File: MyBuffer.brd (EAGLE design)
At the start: 60 x 137.5 mm, 72 parts, among them Q1 BD140, Q2 BD139, Q3 BD140, Q4 BD139, T10 BD140, T11 BD139, T12 BD140, T9 BD139

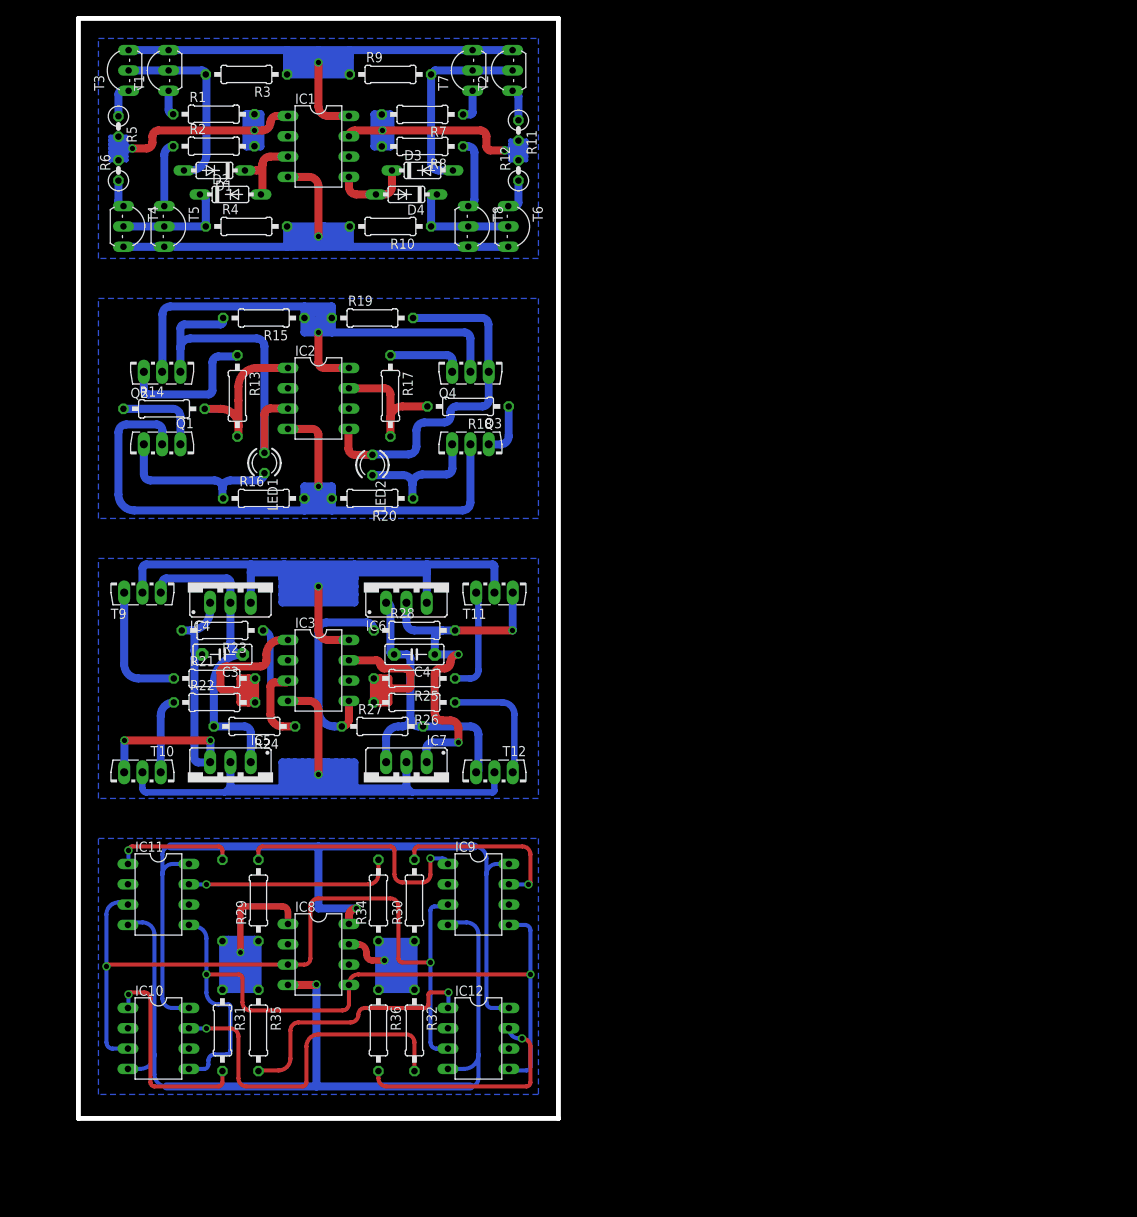
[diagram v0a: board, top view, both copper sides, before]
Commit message: add module capacitance multiplier and buffer ground
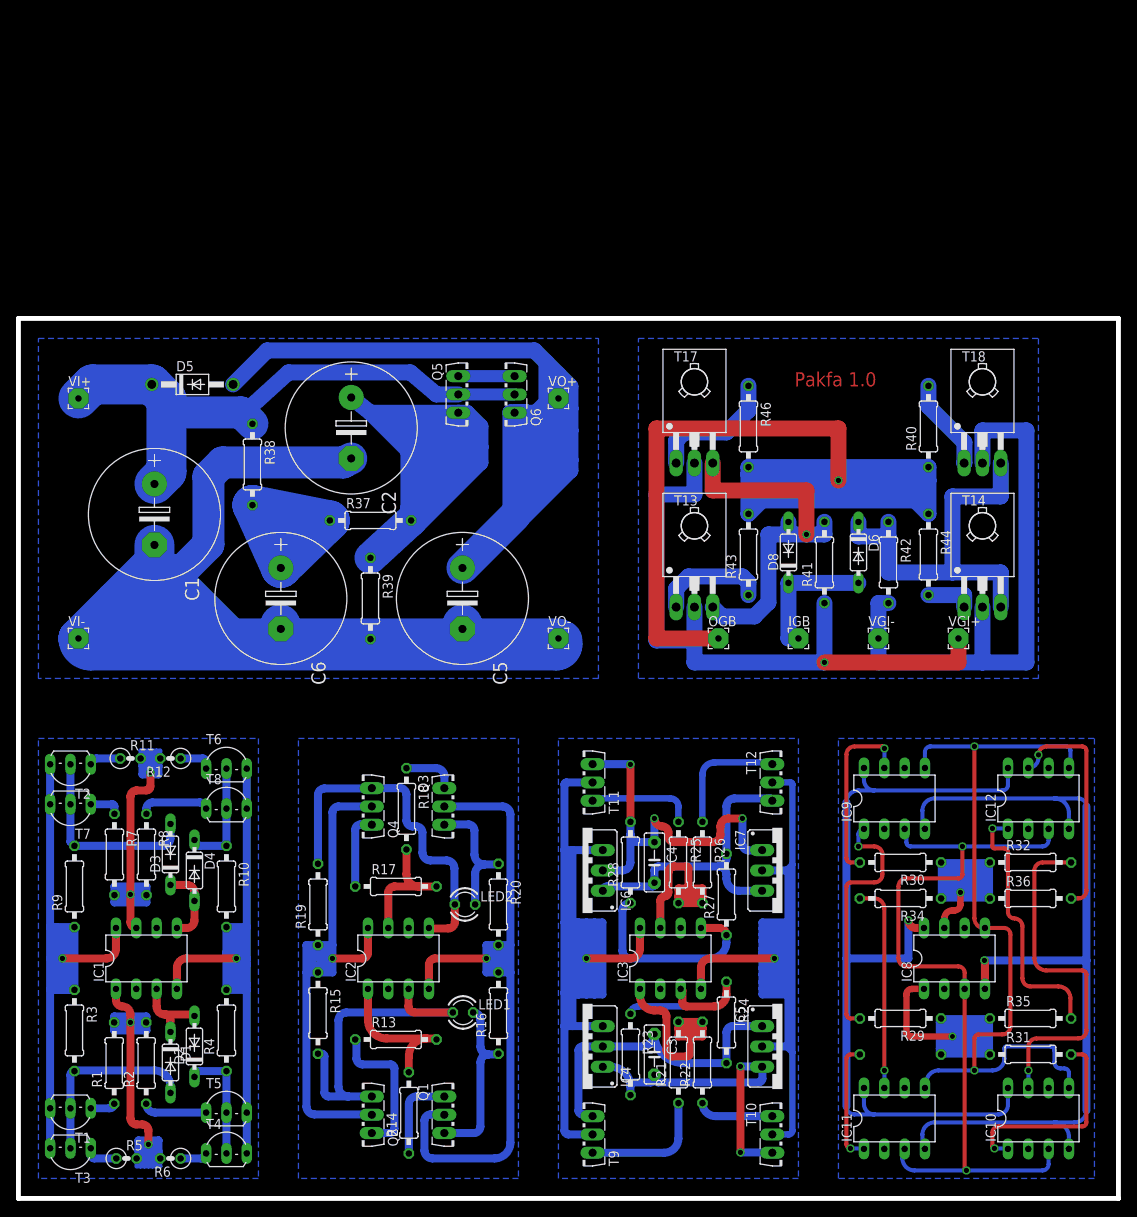
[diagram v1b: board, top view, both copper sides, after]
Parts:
- added C1: 2200uf, rcl:E7,5-16
- added C2, C5, C6: 470uf, rcl:E7,5-16
- added D5: 1N4004, diode:DO41-10
- added D6, D8: 1N4148DO35-7, diode:DO35-7
- added IGB, OGB, VGI+, VGI-, VI+, VI-, VO+, VO-: (no value), wirepad:2,54/0,8
- added Q5, Q6: BD139, transistor-power:TO126AV
- added R37, R38: 220, resistor:0207/10
- added R39: 12k, resistor:0207/10
- added R40, R43, R44, R46: 10, resistor:0207/10
- added R41, R42: 2k, resistor:0207/10
- added T13, T17: BD139, transistor-npn:TO126
- added T14, T18: BD140, transistor-pnp:TO126
- moved T3 136.1 mm to (-1.00, -5.00), turned to 180 degrees
- moved T1 131.5 mm to (-1.00, 0.00), turned to 180 degrees
- moved R5 129.0 mm to (6.00, -5.00), turned to 0 degrees
- moved R6 123.7 mm to (11.5, -5.00), turned to 180 degrees
- moved R3 121.4 mm to (-0.50, 11.0), turned to 270 degrees
- moved R1 119.3 mm to (4.47, 6.92), turned to 90 degrees
- moved T4 115.2 mm to (18.5, -3.10), turned to 0 degrees
- moved R2 114.9 mm to (8.47, 6.92), turned to 90 degrees
- moved D1 111.6 mm to (11.5, 7.00), turned to 270 degrees
- moved IC10 110.5 mm to (120.0, 0.00), turned to 0 degrees
- moved T5 109.7 mm to (18.5, 2.00), turned to 0 degrees
- moved R9 108.9 mm to (-0.50, 29.0), turned to 90 degrees
- moved D2 106.6 mm to (14.5, 9.00), turned to 90 degrees
- moved T7 105.1 mm to (-1.00, 38.0), turned to 180 degrees
- moved IC1 103.8 mm to (8.50, 20.0), turned to 0 degrees
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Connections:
- new net N$32: C2.+, Q5.B, R37.2, R39.1
- new net N$33: Q5.E, Q6.B
- new net N$35: C6.+, R37.1, R38.2
- new net N$36: C1.+, D5.C, Q5.C, Q6.C, R38.1, VI+.1
- new net N$37: C1.-, C2.-, C5.-, C6.-, R39.2, VI-.1, VO-.1
- new net N$39: C5.+, D5.A, Q6.E, VO+.1
- new net N$40: OGB.1, R40.1, R43.2, R44.1, R46.2
- new net N$42: R46.1, T17.1
- new net N$44: R40.2, T18.1
- new net N$45: D6.C, R42.1, T14.3, T18.3
- new net N$46: D8.A, R41.2, T13.3, T17.3
- new net N$48: R41.1, T13.2, T17.2, VGI+.1
- new net N$50: R42.2, T14.2, T18.2, VGI-.1
- new net N$51: D6.A, D8.C, IGB.1
- new net N$52: R43.1, T13.1
- new net N$54: R44.2, T14.1
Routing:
- net N$37: track 0.00 -> 240.7 mm
- net N$39: track 0.00 -> 173.8 mm
- net N$40: track 0.00 -> 166.1 mm, vias 0 -> 1
- net N$32: track 0.00 -> 128.7 mm
- net N$48: track 0.00 -> 82.0 mm, vias 0 -> 1
- net N$36: track 0.00 -> 72.9 mm
- net N$50: track 0.00 -> 72.7 mm
- net N$45: track 0.00 -> 50.0 mm
- net N$46: track 0.00 -> 47.4 mm, vias 0 -> 1
- net N$35: track 0.00 -> 33.0 mm
- net N$51: track 0.00 -> 16.9 mm
- net N$42: track 0.00 -> 16.5 mm
- net N$52: track 0.00 -> 13.9 mm
- net N$44: track 0.00 -> 11.5 mm
- net OUTBUFFER1LEFT: track 63.5 -> 72.0 mm
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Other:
- board size 60 x 137.5 mm -> 137.5 x 110 mm
- board text added: "Pakfa 1.0"

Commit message: Initial Commit
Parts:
- T13, T17: device transistor-npn:TO126 -> transistor-power:TO126AV
- T14, T18: device transistor-pnp:TO126 -> transistor-power:TO126AV
- moved T3 136.1 mm to (5.00, 131.0), turned to 90 degrees
- moved T1 131.5 mm to (10.0, 131.0), turned to 90 degrees
- moved R5 129.0 mm to (5.00, 124.0), turned to 270 degrees
- moved R6 123.7 mm to (5.00, 118.5), turned to 90 degrees
- moved R3 121.4 mm to (21.0, 130.5), turned to 180 degrees
- moved R1 119.3 mm to (16.9, 125.5), turned to 0 degrees
- moved T4 115.2 mm to (6.90, 111.5), turned to 270 degrees
- moved R2 114.9 mm to (16.9, 121.5), turned to 0 degrees
- moved D1 111.6 mm to (17.0, 118.5), turned to 180 degrees
- moved IC10 110.5 mm to (10.0, 10.0), turned to 270 degrees
- moved T5 109.7 mm to (12.0, 111.5), turned to 270 degrees
- moved R9 108.9 mm to (39.0, 130.5), turned to 0 degrees
- moved VI+ 108.3 mm to (100.0, 131.5), turned to 270 degrees
- moved D2 106.6 mm to (19.0, 115.5), turned to 0 degrees
- moved T7 105.1 mm to (48.0, 131.0), turned to 90 degrees
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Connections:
- net N$42: now also T17.E; no longer T17.1
- net N$44: now also T18.E; no longer T18.1
- net N$45: now also T14.B, T18.B; no longer T14.3, T18.3
- net N$46: now also T13.B, T17.B; no longer T13.3, T17.3
- net N$48: now also T13.C, T17.C; no longer T13.2, T17.2
- net N$50: now also T14.C, T18.C; no longer T14.2, T18.2
- net N$52: now also T13.E; no longer T13.1
- net N$54: now also T14.E; no longer T14.1
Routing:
- net N$61: track 0.00 -> 418.5 mm
- net N$59: track 0.00 -> 227.0 mm
- net N$60: track 0.00 -> 190.0 mm
- net N$58: track 0.00 -> 182.0 mm
- net N$57: track 0.00 -> 180.0 mm
- net N$56: track 0.00 -> 173.0 mm
- net N$55: track 0.00 -> 173.0 mm
- net N$45: track 50.0 -> 129.9 mm
- net N$40: track 166.1 -> 216.8 mm
- net N$42: track 16.5 -> 56.5 mm
- net N$52: track 13.9 -> 53.3 mm
- net N$48: track 82.0 -> 118.3 mm
- net N$44: track 11.5 -> 36.0 mm
- net N$51: track 16.9 -> 39.5 mm
- net N$50: track 72.7 -> 94.6 mm
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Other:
- board size 137.5 x 110 mm -> 110 x 137.5 mm
- board text added: "BUFFER"
- board text removed: "Pakfa 1.0"
